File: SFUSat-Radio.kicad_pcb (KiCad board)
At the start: 4 copper layers, 95.9 x 90.2 mm, 284 parts, among them J1 PC104-8BIT, J10 TP_TH_150, J11 TP_TH_150, J12 SMA, J13 SMA, J14 SMA, J15 Conn_01x02, J16 SMA, J17 SMA, J18 SMA, J19 Conn_01x03, J2 PC104PTH, J20 Conn_01x03, J21 TP_TH_150, J22 TP_TH_150, J23 TP_TH_150, J24 TP_TH_150, J25 Conn_01x02, J3 PC104PTH, J4 PC104PTH, J400 SMA, J401 TP_TH_150, J402 TP_TH_150, J404 TP_TH_150, J405 TP_TH_150, J406 TP_TH_150, J5 PC104PTH, J500 SMA, J501 TP_TH_150, J502 TP_TH_150, J504 TP_TH_150, J505 TP_TH_150, J506 TP_TH_150, J6 SMA, J7 TP_TH_150, J8 TP_TH_150, J9 TP_TH_150, P1 3pin-DC-power, U1 SINGLE_0402, U10 TPS799, U100 CC1101-Q1, U101 0433BM15A0001, U11 SINGLE_0402, U110 CC1101-Q1, U111 0915BM15A0001E, U12 CONN_02X05_SHRD, U13 CONN_02X05_SHRD, U14 2N7002DW, U15 TPS62175DQCR, U16 TPS71750DSER, U17 74LVC1G14SE-7, U2 SKY13345-368LF, U3 CD4555BPWR, U4 LMS3635AQRNLRQ1, U400 SINGLE_0402, U401 LMV358, U402 RF6886, U420 2N7002DW, U5 MML09211H, U500 SINGLE_0402, U501 LMV358, U502 RF6886, U6 SINGLE_0402, U600 STLM75, U610 STLM75, U7 SKY13372-467LF, U8 SINGLE_0402, U9 TLV702, X100 NX3225GA, X110 NX3225GA

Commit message: Major floods added
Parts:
- moved C40 2.59 mm to (166.4, 83.8), turned to 0 degrees
- moved C402 0.40 mm to (149.3, 135.4)
- moved C411 0.39 mm to (150.4, 136.3)
- moved C410 0.39 mm to (150.4, 133.6)
- moved R409 0.38 mm to (150.9, 135.0)
- moved C409 0.12 mm to (152.4, 134.2)
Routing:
- net /5V0: track 12.1 -> 98.0 mm, vias 2 -> 6
- net /SCL: track 58.2 -> 121.9 mm
- net /SDA: track 59.6 -> 113.7 mm
- net /3V1: track 128.1 -> 174.8 mm, vias 2 -> 3
- net /3V3: track 84.4 -> 41.3 mm, vias 27 -> 18
- net /PKT_RCV: track 6.48 -> 25.6 mm
- net /3V6: track 105.2 -> 99.9 mm, vias 14 -> 20
- net /UB_LP: track 42.9 -> 41.5 mm
- net /PA_LB/VREG: track 40.3 -> 40.9 mm
- net GND: track 120.4 -> 120.1 mm, vias 96 -> 105
- added copper zone on F.Cu, net /5V0
- removed copper zone on B.Cu, net /3V3

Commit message: Some more routing
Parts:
- moved J11 4.83 mm to (157.6, 61.8)
- moved P1 4.76 mm to (151.1, 62.8)
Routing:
- net Net-(R16-Pad2): track 12.7 -> 13.8 mm
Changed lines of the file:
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@@
   (general
     (links 732)
-    (no_connects 52)
+    (no_connects 50)
     (area 45.1 57.330476 358.142847 159.700001)
     (thickness 1.6)
     (drawings 26)
-    (tracks 1361)
+    (tracks 1362)
     (zones 0)
     (modules 284)
@@
   )
   (setup
-    (last_trace_width 0.254)
+    (last_trace_width 0.2)
     (user_trace_width 0.1524)
     (user_trace_width 0.2)
@@
   )
   (module SFUSat:TP_TH_150 (layer F.Cu)
-    (at 152.75 61.75)
+    (at 157.58 61.82)
     (fp_text reference J11 (at 0 -2) (layer F.SilkS) hide
       (effects (font (size 1 1) (thickness 0.15)))
@@
   (module SFUSat:BMI-S-205-F locked (layer F.Cu)
     (at 133.19 89.36 270)
-    (fp_text reference SH500 (at 0 -21.5 270) (layer F.SilkS)
+    (fp_text reference SH500 (at 0 -21.5 270) (layer F.SilkS) hide
       (effects (font (size 1 1) (thickness 0.15)))
     )
@@
   (module SFUSat:BMI-S-205-F locked (layer F.Cu)
     (at 151.2 134.245 270)
-    (fp_text reference SH400 (at 0 -21.5 270) (layer F.SilkS)
+    (fp_text reference SH400 (at 0 -21.5 270) (layer F.SilkS) hide
       (effects (font (size 1 1) (thickness 0.15)))
     )
@@
   (module SFUSat:PESD57zx (layer F.Cu)
     (at 160.87 144.02 270)
-    (fp_text reference D401 (at 0 -1.5 270) (layer F.SilkS)
+    (fp_text reference D401 (at 0 1.39 270) (layer F.SilkS)
       (effects (font (size 1 1) (thickness 0.15)))
     )
@@
   (module SFUSat:NX3225GA (layer F.Cu)
     (at 171.87 105.03 90)
-    (fp_text reference X100 (at 0 2.35 90) (layer F.SilkS)
+    (fp_text reference X100 (at 0 -2.32 90) (layer F.SilkS)
       (effects (font (size 1 1) (thickness 0.15)))
     )
@@
   (module SFUSat:TSSOP-16 (layer F.Cu)
     (at 124.77 132.47 90)
-    (fp_text reference U3 (at 3.6 0 180) (layer F.SilkS)
+    (fp_text reference U3 (at 3.28 0.01 180) (layer F.SilkS)
       (effects (font (size 1 1) (thickness 0.15)))
     )
@@
     (tags "resistor 0402")
     (attr smd)
-    (fp_text reference R615 (at 0 -1.35 90) (layer F.SilkS)
+    (fp_text reference R615 (at 3.68 0 90) (layer F.SilkS)
       (effects (font (size 1 1) (thickness 0.15)))
     )
@@
     (tags "resistor 0402")
     (attr smd)
-    (fp_text reference R612 (at 0 -1.35 270) (layer F.SilkS)
+    (fp_text reference R612 (at -3.68 0.02 270) (layer F.SilkS)
       (effects (font (size 1 1) (thickness 0.15)))
     )
@@
     (tags "resistor 0402")
     (attr smd)
-    (fp_text reference R611 (at 0 -1.35 90) (layer F.SilkS)
+    (fp_text reference R611 (at 3.68 -0.01 90) (layer F.SilkS)
       (effects (font (size 1 1) (thickness 0.15)))
     )
@@
     (tags "resistor 0402")
     (attr smd)
-    (fp_text reference R410 (at 0 -1.35 270) (layer F.SilkS)
+    (fp_text reference R410 (at 0.01 -1.36 270) (layer F.SilkS)
       (effects (font (size 1 1) (thickness 0.15)))
     )
@@
     (tags "resistor 0402")
     (attr smd)
-    (fp_text reference R100 (at 0 -1.35) (layer F.SilkS)
+    (fp_text reference R100 (at 4.2 -0.01) (layer F.SilkS)
       (effects (font (size 1 1) (thickness 0.15)))
     )
@@
   (module SFUSat:UFL-R-SMT-1-Coaxial-Connector (layer F.Cu)
     (at 184.97 128 225)
-    (fp_text reference J18 (at 0 2.8 225) (layer F.SilkS)
+    (fp_text reference J18 (at -0.007071 -2.425376 225) (layer F.SilkS)
       (effects (font (size 1 1) (thickness 0.15)))
     )
@@
     (tags "capacitor 0402")
     (attr smd)
-    (fp_text reference C610 (at 0 -1.9 180) (layer F.SilkS)
+    (fp_text reference C610 (at -0.02 -1.24 180) (layer F.SilkS)
       (effects (font (size 1 1) (thickness 0.15)))
     )
@@
     (tags "capacitor 0402")
     (attr smd)
-    (fp_text reference C104 (at 0 -1.9 180) (layer F.SilkS)
+    (fp_text reference C104 (at -4.16 0 180) (layer F.SilkS)
       (effects (font (size 1 1) (thickness 0.15)))
     )
@@
     (tags "capacitor 0402")
     (attr smd)
-    (fp_text reference C103 (at 0 -1.9 180) (layer F.SilkS)
+    (fp_text reference C103 (at -4.2 0 180) (layer F.SilkS)
       (effects (font (size 1 1) (thickness 0.15)))
     )
@@
     (tags "capacitor 0402")
     (attr smd)
-    (fp_text reference C102 (at 0 -1.9 180) (layer F.SilkS)
+    (fp_text reference C102 (at 0 -1.26 180) (layer F.SilkS)
       (effects (font (size 1 1) (thickness 0.15)))
     )
@@
     (tags "capacitor 0402")
     (attr smd)
-    (fp_text reference C13 (at 0 -1.9) (layer F.SilkS)
+    (fp_text reference C13 (at 3.48 0) (layer F.SilkS)
       (effects (font (size 1 1) (thickness 0.15)))
     )
@@
     (tags "capacitor 0402")
     (attr smd)
-    (fp_text reference C14 (at 0 -1.9 45) (layer F.SilkS)
+    (fp_text reference C14 (at 0 -1.131371 45) (layer F.SilkS)
       (effects (font (size 1 1) (thickness 0.15)))
     )
@@
   (module SFUSat:SMA-Vert-TH locked (layer F.Cu)
     (at 121.92 121.5 90)
-    (fp_text reference J6 (at 0 5.6 90) (layer F.SilkS)
+    (fp_text reference J6 (at 0 4.18 90) (layer F.SilkS)
       (effects (font (size 1 1) (thickness 0.15)))
     )
@@
   (module SFUSat:SOT353 (layer F.Cu)
     (at 185.43 112.82 180)
-    (fp_text reference U17 (at 0 -2.5 180) (layer F.SilkS)
+    (fp_text reference U17 (at -2.94 0 180) (layer F.SilkS)
       (effects (font (size 1 1) (thickness 0.15)))
     )
@@
     (tags "capacitor 0402")
     (attr smd)
-    (fp_text reference C42 (at 0 -1.9) (layer F.SilkS)
+    (fp_text reference C42 (at 2.54 0) (layer F.SilkS)
       (effects (font (size 1 1) (thickness 0.15)))
     )
@@
     (tags "resistor 0402")
     (attr smd)
-    (fp_text reference R610 (at 0 -1.35 270) (layer F.SilkS)
+    (fp_text reference R610 (at -3.68 -0.05 270) (layer F.SilkS)
       (effects (font (size 1 1) (thickness 0.15)))
     )
@@
     (tags "resistor 0402")
     (attr smd)
-    (fp_text reference R613 (at 0 -1.35 90) (layer F.SilkS)
+    (fp_text reference R613 (at 3.68 0 90) (layer F.SilkS)
       (effects (font (size 1 1) (thickness 0.15)))
     )
@@
     (tags "resistor 0402")
     (attr smd)
-    (fp_text reference R614 (at -0.648571 -2.625 270) (layer F.SilkS)
+    (fp_text reference R614 (at 0 -1.37 270) (layer F.SilkS)
       (effects (font (size 1 1) (thickness 0.15)))
     )
@@
     (tags "resistor 0402")
     (attr smd)
-    (fp_text reference R411 (at 0 -1.35 90) (layer F.SilkS)
+    (fp_text reference R411 (at 0 1.36 90) (layer F.SilkS)
       (effects (font (size 1 1) (thickness 0.15)))
     )
@@
   )
   (module SFUSat:PJ-028-SMT-TR-3pin-DC-jack (layer F.Cu)
-    (at 146.36 62.84 270)
-    (fp_text reference P1 (at 9.5 1 360) (layer F.SilkS)
+    (at 151.12 62.81 270)
+    (fp_text reference P1 (at -3.25 4.9 360) (layer F.SilkS)
       (effects (font (size 1 1) (thickness 0.15)))
     )
@@
       (net 183 /VIN))
   )
-  (gr_text GND (at 149.25 61.75 180) (layer F.SilkS)
+  (gr_text GND (at 154.01 61.72 180) (layer F.SilkS)
     (effects (font (size 1 1) (thickness 0.15)))
   )
@@
   (segment (start 165.45 74.04) (end 165.45 75.04) (width 0.254) (layer F.Cu) (net 131))
   (via (at 165.45 75.04) (size 0.6) (drill 0.4) (layers F.Cu B.Cu) (net 131))
+  (segment (start 167.2 74.29) (end 167.2 75.34) (width 0.254) (layer F.Cu) (net 132))
   (segment (start 156.45 73.79) (end 156.65 73.79) (width 0.254) (layer F.Cu) (net 132))
   (segment (start 156.65 73.79) (end 157.2 74.34) (width 0.254) (layer F.Cu) (net 132))
@@
   (segment (start 182.42 96.13) (end 182.82 95.73) (width 0.2) (layer F.Cu) (net 170))
   (segment (start 182.82 95.73) (end 184.095 95.73) (width 0.2) (layer F.Cu) (net 170))
-  (segment (start 147.96 65.59) (end 147.96 64.43) (width 0.254) (layer F.Cu) (net 183))
-  (via (at 147.96 64.43) (size 0.6) (drill 0.4) (layers F.Cu B.Cu) (net 183))
-  (segment (start 147.96 66.84) (end 147.96 65.59) (width 0.254) (layer F.Cu) (net 183))
-  (via (at 147.96 65.59) (size 0.6) (drill 0.4) (layers F.Cu B.Cu) (net 183))
-  (segment (start 147.96 68.34) (end 147.96 66.84) (width 0.254) (layer F.Cu) (net 183))
-  (via (at 147.96 66.84) (size 0.6) (drill 0.4) (layers F.Cu B.Cu) (net 183))
+  (segment (start 152.72 65.56) (end 152.72 64.4) (width 0.254) (layer F.Cu) (net 183))
+  (via (at 152.72 64.4) (size 0.6) (drill 0.4) (layers F.Cu B.Cu) (net 183))
+  (segment (start 152.72 66.81) (end 152.72 65.56) (width 0.254) (layer F.Cu) (net 183))
+  (via (at 152.72 65.56) (size 0.6) (drill 0.4) (layers F.Cu B.Cu) (net 183))
+  (segment (start 152.72 68.31) (end 152.72 66.81) (width 0.254) (layer F.Cu) (net 183))
+  (via (at 152.72 66.81) (size 0.6) (drill 0.4) (layers F.Cu B.Cu) (net 183))
   (segment (start 163.8 63.54) (end 160.29 63.54) (width 0.508) (layer F.Cu) (net 183))
   (segment (start 160.29 63.54) (end 160.25 63.5) (width 0.508) (layer F.Cu) (net 183))
@@
       (pts
         (xy 192.75 69.25) (xy 169.5 69.25) (xy 169.5 69.75) (xy 169.5 84.25) (xy 155.75 84.25)
-        (xy 155.76 69.33) (xy 146.76 69.34) (xy 146.76 58.25) (xy 192.5 58.25) (xy 192.75 58.25)
+        (xy 155.76 69.33) (xy 151.52 69.32) (xy 151.52 58.23) (xy 192.5 58.25) (xy 192.75 58.25)
       )
     )
@@
     (polygon
       (pts
-        (xy 146.76 64.1) (xy 149.16 64.1) (xy 149.16 69.34) (xy 146.76 69.34)
+        (xy 151.52 64.07) (xy 153.92 64.07) (xy 153.92 69.31) (xy 151.52 69.31)
       )
     )

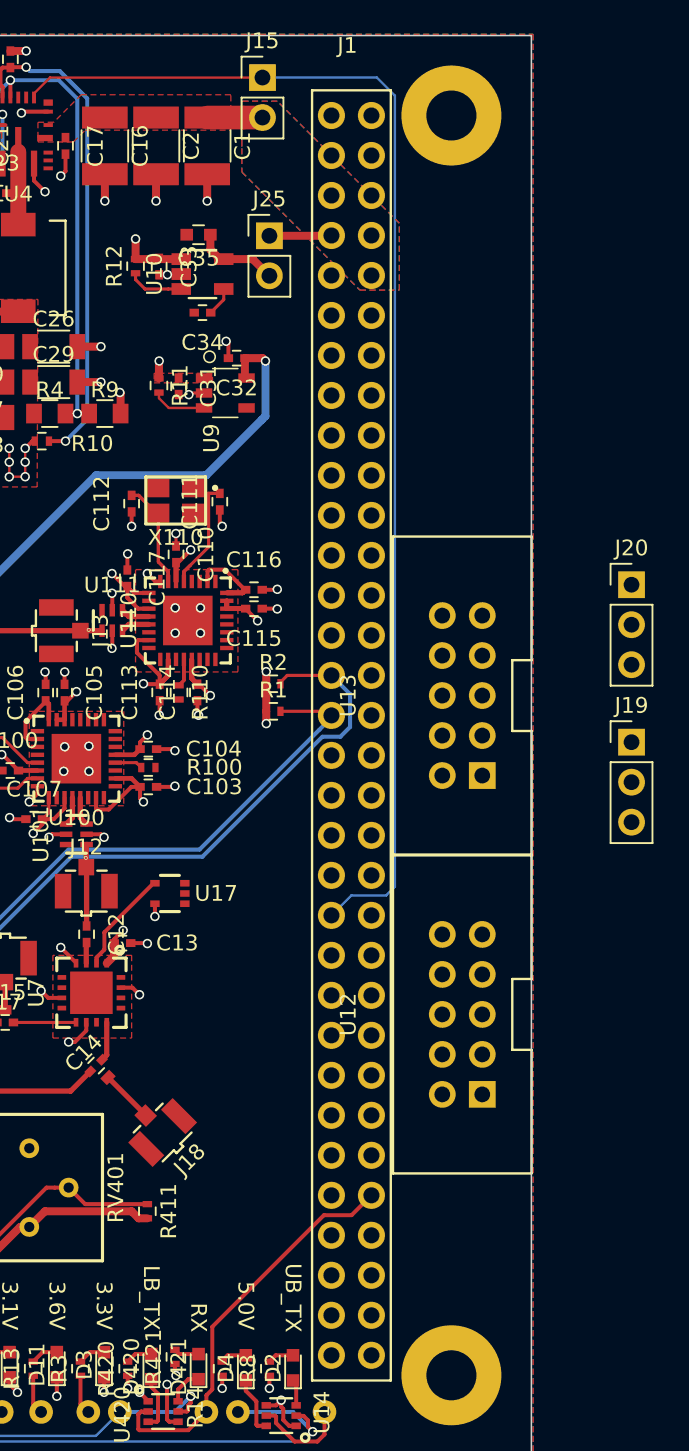
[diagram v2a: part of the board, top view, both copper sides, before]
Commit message: removed op_3v3, routed SPI
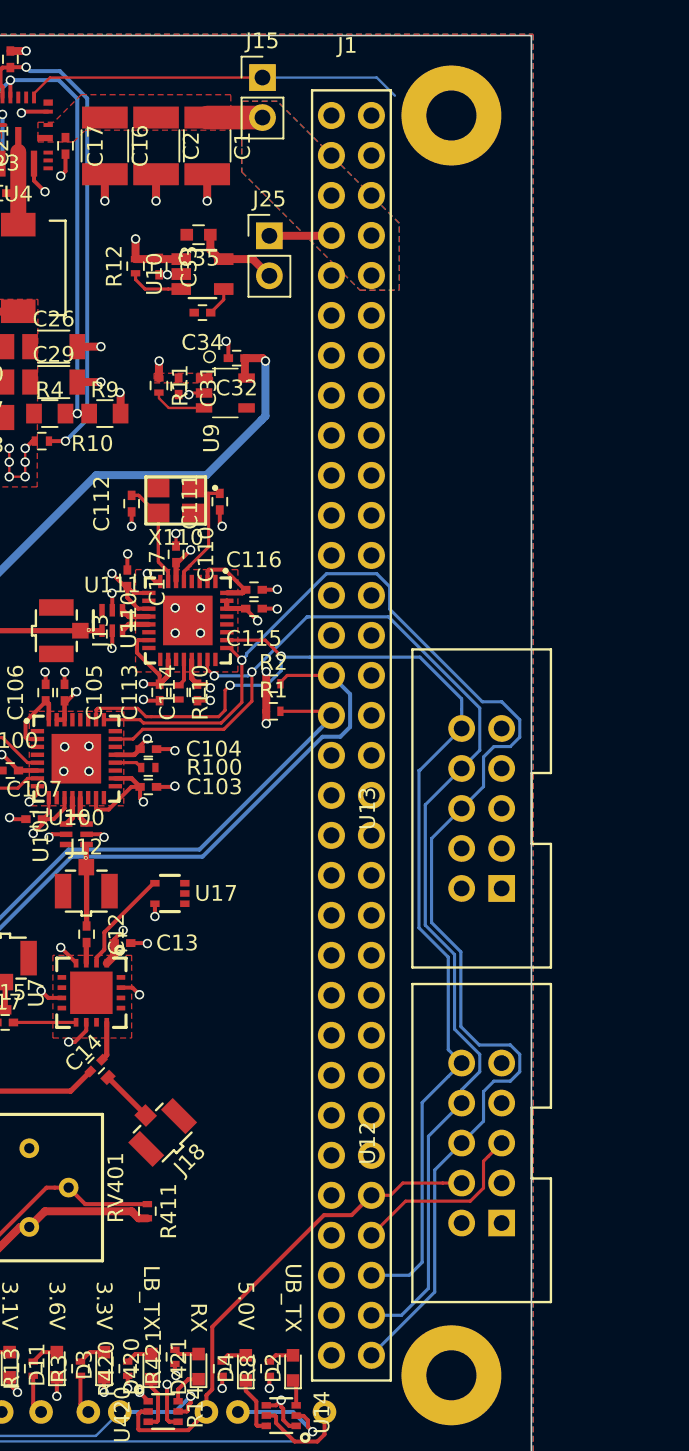
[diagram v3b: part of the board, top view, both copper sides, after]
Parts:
- removed J19, J20: Conn_01x03, Socket_Strips:Socket_Strip_Straight_1x03_Pitch2.54mm
- moved U12 8.26 mm to (205.2, 128.7)
- moved U13 7.27 mm to (205.2, 107.4)
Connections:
- C100 pad 2: /CC1101_LB/VDD_3.3 -> /3V3
- C103 pad 2: /CC1101_LB/VDD_3.3 -> /3V3
- C104 pad 2: /CC1101_LB/VDD_3.3 -> /3V3
- C105 pad 2: /CC1101_LB/VDD_3.3 -> /3V3
- C107 pad 2: /CC1101_LB/VDD_3.3 -> /3V3
- C110 pad 2: /CC1101_UB/VDD_3.3 -> /3V3
- C113 pad 2: /CC1101_UB/VDD_3.3 -> /3V3
- C114 pad 2: /CC1101_UB/VDD_3.3 -> /3V3
- C115 pad 2: /CC1101_UB/VDD_3.3 -> /3V3
- C117 pad 2: /CC1101_UB/VDD_3.3 -> /3V3
- U100 pad 11: /CC1101_LB/VDD_3.3 -> /3V3
- U100 pad 15: /CC1101_LB/VDD_3.3 -> /3V3
- U100 pad 18: /CC1101_LB/VDD_3.3 -> /3V3
- U100 pad 21: /CC1101_LB/VDD_3.3 -> /3V3
- U100 pad 30: /CC1101_LB/VDD_3.3 -> /3V3
- U100 pad 31: /CC1101_LB/VDD_3.3 -> /3V3
- U100 pad 6: /CC1101_LB/VDD_3.3 -> /3V3
- U100 pad 9: /CC1101_LB/VDD_3.3 -> /3V3
- U110 pad 11: /CC1101_UB/VDD_3.3 -> /3V3
- U110 pad 15: /CC1101_UB/VDD_3.3 -> /3V3
- U110 pad 18: /CC1101_UB/VDD_3.3 -> /3V3
- U110 pad 21: /CC1101_UB/VDD_3.3 -> /3V3
- U110 pad 30: /CC1101_UB/VDD_3.3 -> /3V3
- U110 pad 31: /CC1101_UB/VDD_3.3 -> /3V3
- U110 pad 6: /CC1101_UB/VDD_3.3 -> /3V3
- U110 pad 9: /CC1101_UB/VDD_3.3 -> /3V3
- U12 pad 2: /CC1101_LB/VDD_3.3 -> /3V3
- U13 pad 2: /CC1101_UB/VDD_3.3 -> /3V3
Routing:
- net /SCLK: track 0.00 -> 89.3 mm, vias 0 -> 1
- net /MOSI: track 0.00 -> 79.0 mm, vias 0 -> 2
- net /MISO: track 0.00 -> 74.6 mm, vias 0 -> 2
- net /EN_3V6: track 79.1 -> 24.1 mm
- net /3V3: track 41.3 -> 89.3 mm, vias 18 -> 28
- net /CC1101_UB/VDD_3.3: track 28.2 -> 0.00 mm, vias 5 -> 0
- net /CC1101_LB/VDD_3.3: track 20.2 -> 0.00 mm, vias 5 -> 0
- net /~LB_CS: track 0.00 -> 11.7 mm
- net /PKT_RCV: track 25.6 -> 31.7 mm

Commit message: routing complete
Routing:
- net /LB_RX0TX1: track 67.7 -> 148.0 mm, vias 2 -> 6
- net /UB_RX0TX1: track 81.5 -> 156.7 mm
- net /~UB_CS: track 0.00 -> 61.3 mm
- net /EN_3V6: track 24.1 -> 80.0 mm, vias 0 -> 1
- net /~LB_CS: track 11.7 -> 63.2 mm, vias 0 -> 2
- net /PKT_RCV: track 31.7 -> 78.3 mm, vias 0 -> 2
- net /CC1101_UB/GDO0: track 0.00 -> 32.3 mm
- net /3V1: track 174.8 -> 175.6 mm
- net Net-(C111-Pad2): track 11.1 -> 10.6 mm
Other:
- net class Default: clearance 0.2 -> 0.1524
- rule trace_clearance: 0.2 -> 0.1524
